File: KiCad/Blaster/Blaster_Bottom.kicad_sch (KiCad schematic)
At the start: 24 parts, among them J2 Power & Output Test Points, J3 Inputs Test Points, Q1 BUK9832-55A, Q2 BUK9832-55A, Q3 BUK9832-55A, U2 PIC16F1788-IP

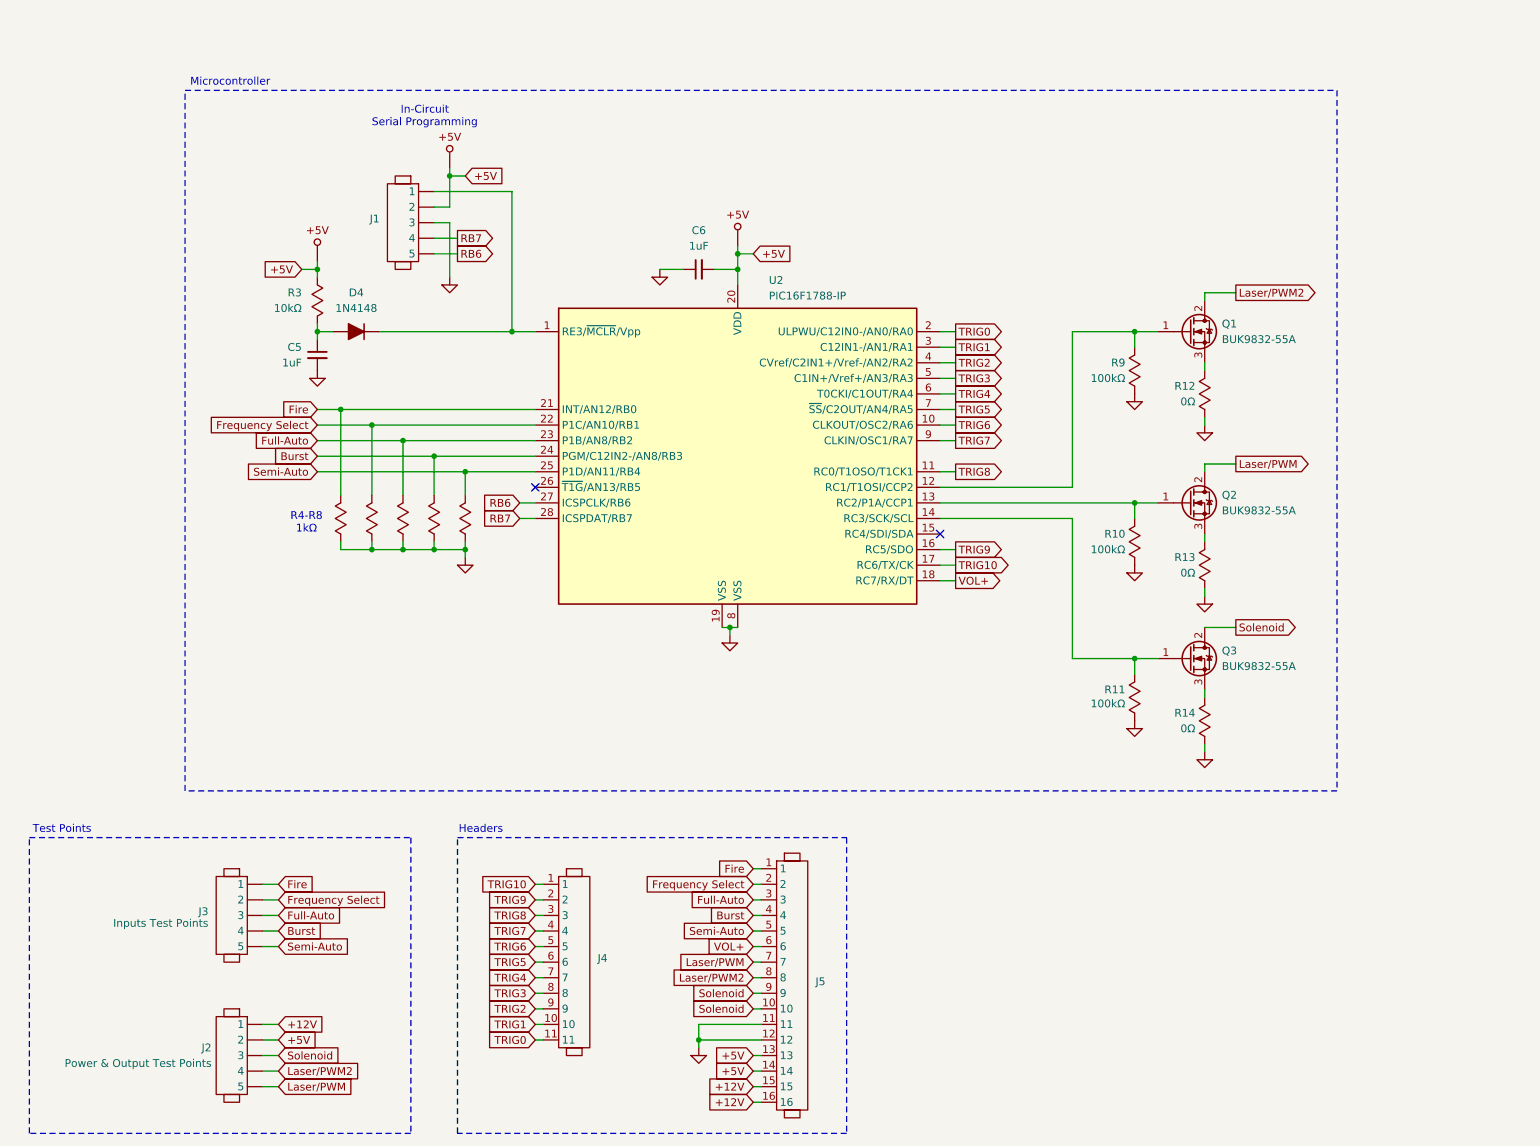
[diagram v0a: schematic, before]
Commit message: Blaster schematic update PIC, solenoid, and FX Mini
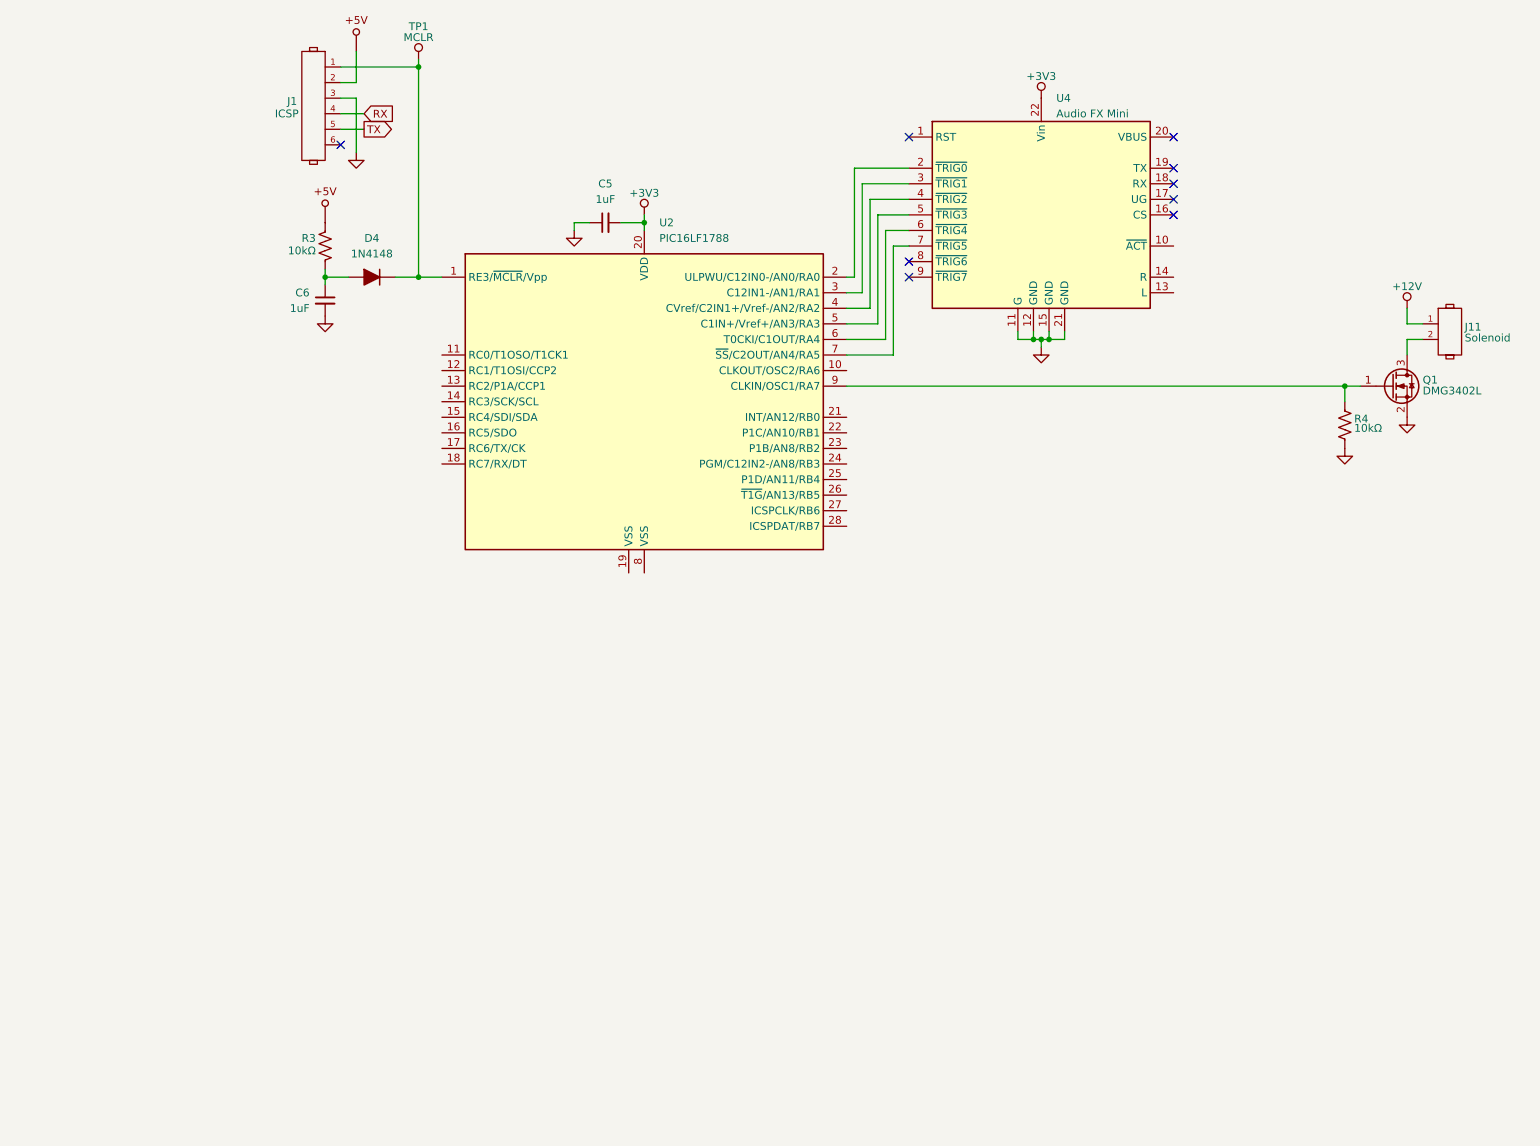
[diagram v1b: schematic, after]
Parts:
- removed J1: ~, Connector_PinHeader_2.54mm:PinHeader_1x05_P2.54mm_Vertical, symbol Libraries:Header_1x5
- removed J2: Power & Output Test Points, Connector_PinHeader_2.54mm:PinHeader_1x05_P2.54mm_Vertical, symbol Libraries:Header_1x5
- removed J3: Inputs Test Points, Connector_PinHeader_2.54mm:PinHeader_1x05_P2.54mm_Vertical, symbol Libraries:Header_1x5
- removed J4: ~, Connector_PinHeader_2.54mm:PinHeader_1x11_P2.54mm_Vertical, symbol Libraries:Header_1x11
- removed J5: ~, Connector_PinHeader_2.54mm:PinHeader_1x16_P2.54mm_Vertical, symbol Libraries:Header_1x16
- removed Q1, Q2, Q3: BUK9832-55A, Package_TO_SOT_SMD:SOT-223-3_TabPin2, symbol Transistor_FET:BUK7880-55A
- removed R10, R11, R9: 100kΩ, Resistor_SMD:R_0805_2012Metric_Pad1.20x1.40mm_HandSolder, symbol Libraries:R_Custom
- removed R12, R13, R14: 0Ω, Resistor_SMD:R_0805_2012Metric_Pad1.20x1.40mm_HandSolder, symbol Libraries:R_Custom
- removed R3: 10kΩ, Resistor_SMD:R_0805_2012Metric_Pad1.20x1.40mm_HandSolder, symbol Libraries:R_Custom
- removed R4, R5, R6, R7, R8: 1kΩ, Resistor_SMD:R_0805_2012Metric_Pad1.20x1.40mm_HandSolder, symbol Libraries:R_Custom
- removed U2: PIC16F1788-IP, AlexWheelockFootprintLibrary:SSOP-28, symbol Libraries:PIC16F883_BIN_ACOUT
- added J1: ICSP, 0_AKeller_Footprints:1x6_100mil_Header, symbol 0_AKeller_Parts:Header_1x6
- added J11: Solenoid, symbol 0_AKeller_Parts:Header_1x2
- added Q1: DMG3402L, Package_TO_SOT_SMD:SOT-23, symbol Transistor_FET:DMG3402L
- added R3, R4: 10kΩ, symbol Device:R_US
- added TP1: MCLR, 0_AKeller_Footprints:1x1_100mil_Header, symbol 0_AKeller_Parts:Test_Point
- added U2: PIC16LF1788, 0_AKeller_Footprints:SSOP-28, symbol Libraries:PIC16F1788
- added U4: Audio FX Mini, symbol 0_AKeller_Parts:FX_Mini
- D4: footprint Diode_SMD:D_0805_2012Metric_Pad1.15x1.40mm_HandSolder -> 0_AKeller_Footprints:Diode_0805
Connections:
- net +12V: now also J11.1
- net +5V: now also J1.2, R3.1; no longer C6.2
- net at D4.1 (K): now also J1.1, TP1.1, U2.1 (RE3/~{MCLR}/Vpp)
- net at C6.1: now also D4.2 (A), R3.2
- net GND: now reaches C5.1
- net GND: now also C6.2, J1.3, Q1.2 (S), R4.2, U4.11 (G), U4.12 (GND), U4.15 (GND), U4.21 (GND); no longer D4.2 (A)
- net +3V3: now reaches C5.2
- net +3V3: now also U2.20 (VDD), U4.22 (Vin)
- new net: U2.2 (ULPWU/C12IN0-/AN0/RA0), U4.2 (~{TRIG0})
- new net: U2.3 (C12IN1-/AN1/RA1), U4.3 (~{TRIG1})
- new net: U2.4 (CVref/C2IN1+/Vref-/AN2/RA2), U4.4 (~{TRIG2})
- new net: U2.5 (C1IN+/Vref+/AN3/RA3), U4.5 (~{TRIG3})
- new net: U2.6 (T0CKI/C1OUT/RA4), U4.6 (~{TRIG4})
- new net: U2.7 (~{SS}/C2OUT/AN4/RA5), U4.7 (~{TRIG5})
- new net: Q1.1 (G), R4.1, U2.9 (CLKIN/OSC1/RA7)
- new net: J11.2, Q1.3 (D)
- new net RX: J1.4
- new net TX: J1.5
- no-connect marks 2 -> 9
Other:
- note removed: "Headers"
- note removed: "In-Circuit Serial Programming"
- note removed: "Microcontroller"
- note removed: "R4-R8 1kΩ"
- note removed: "Test Points"
